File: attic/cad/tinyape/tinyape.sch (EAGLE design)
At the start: 23 parts

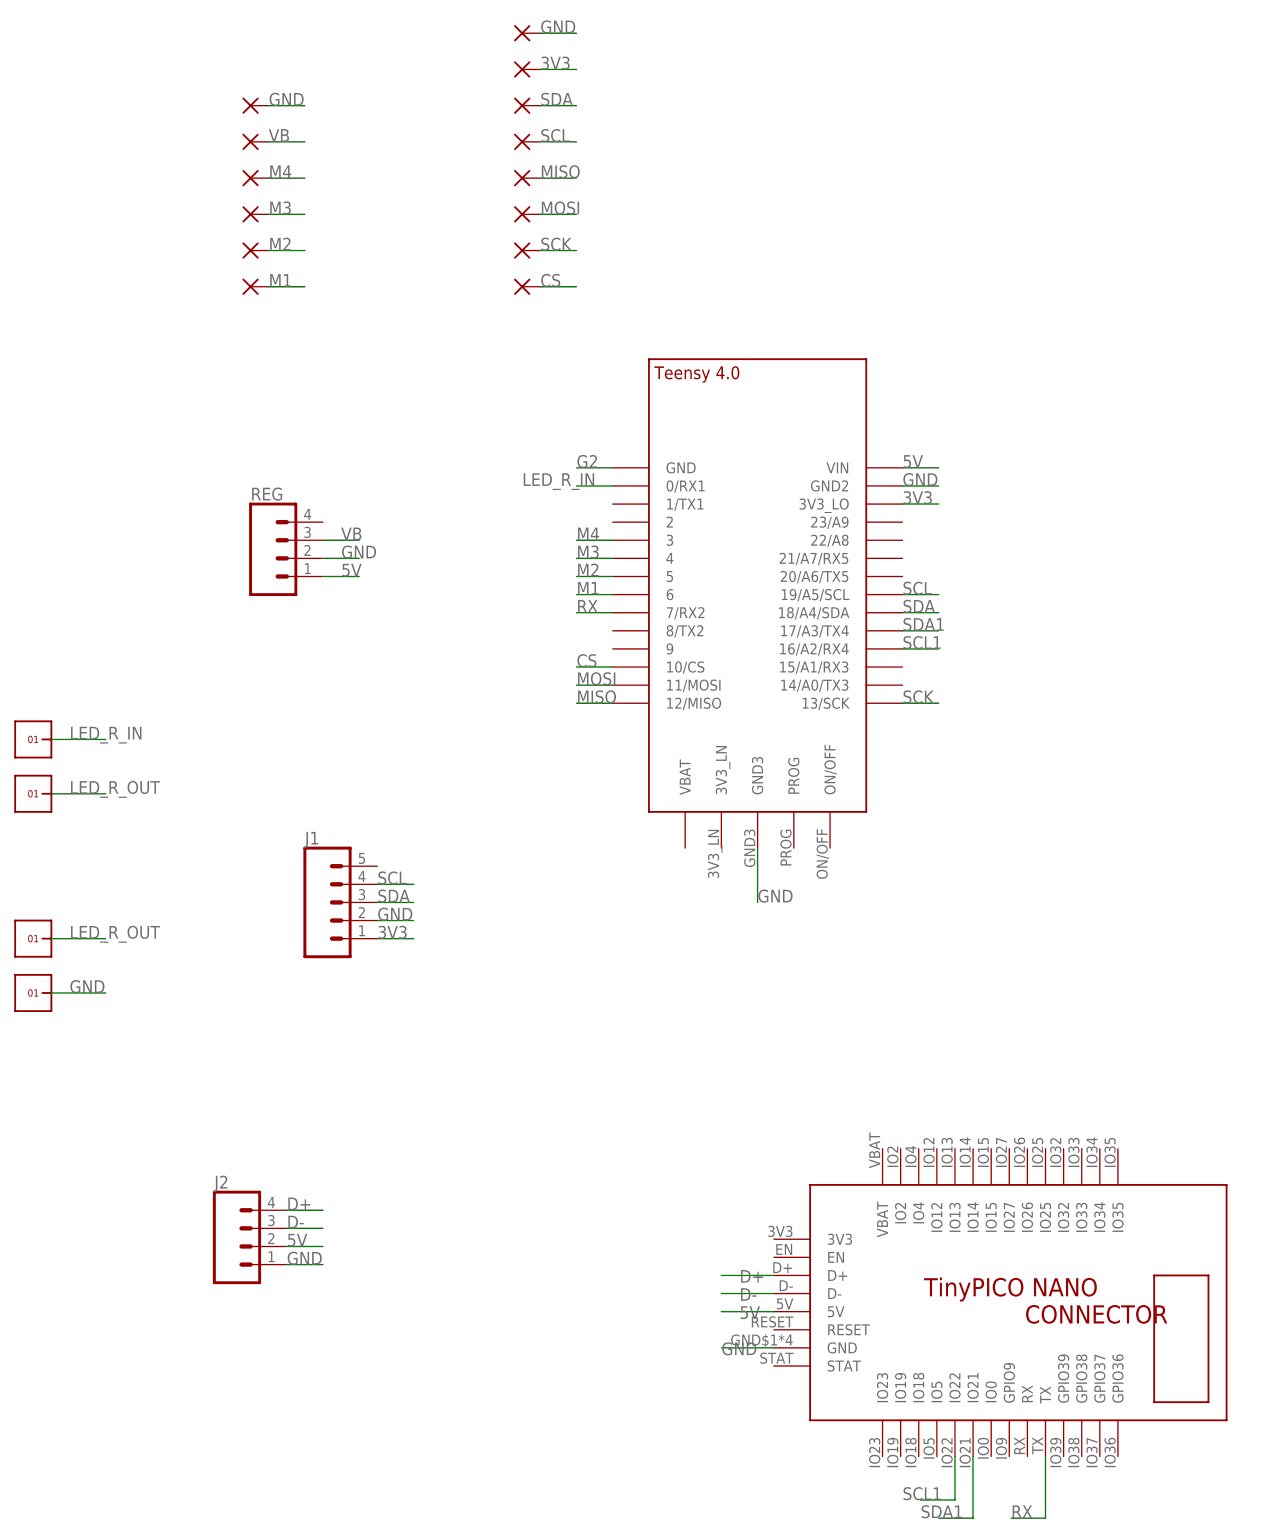
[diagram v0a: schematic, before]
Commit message: new file:   cad/fc.brd
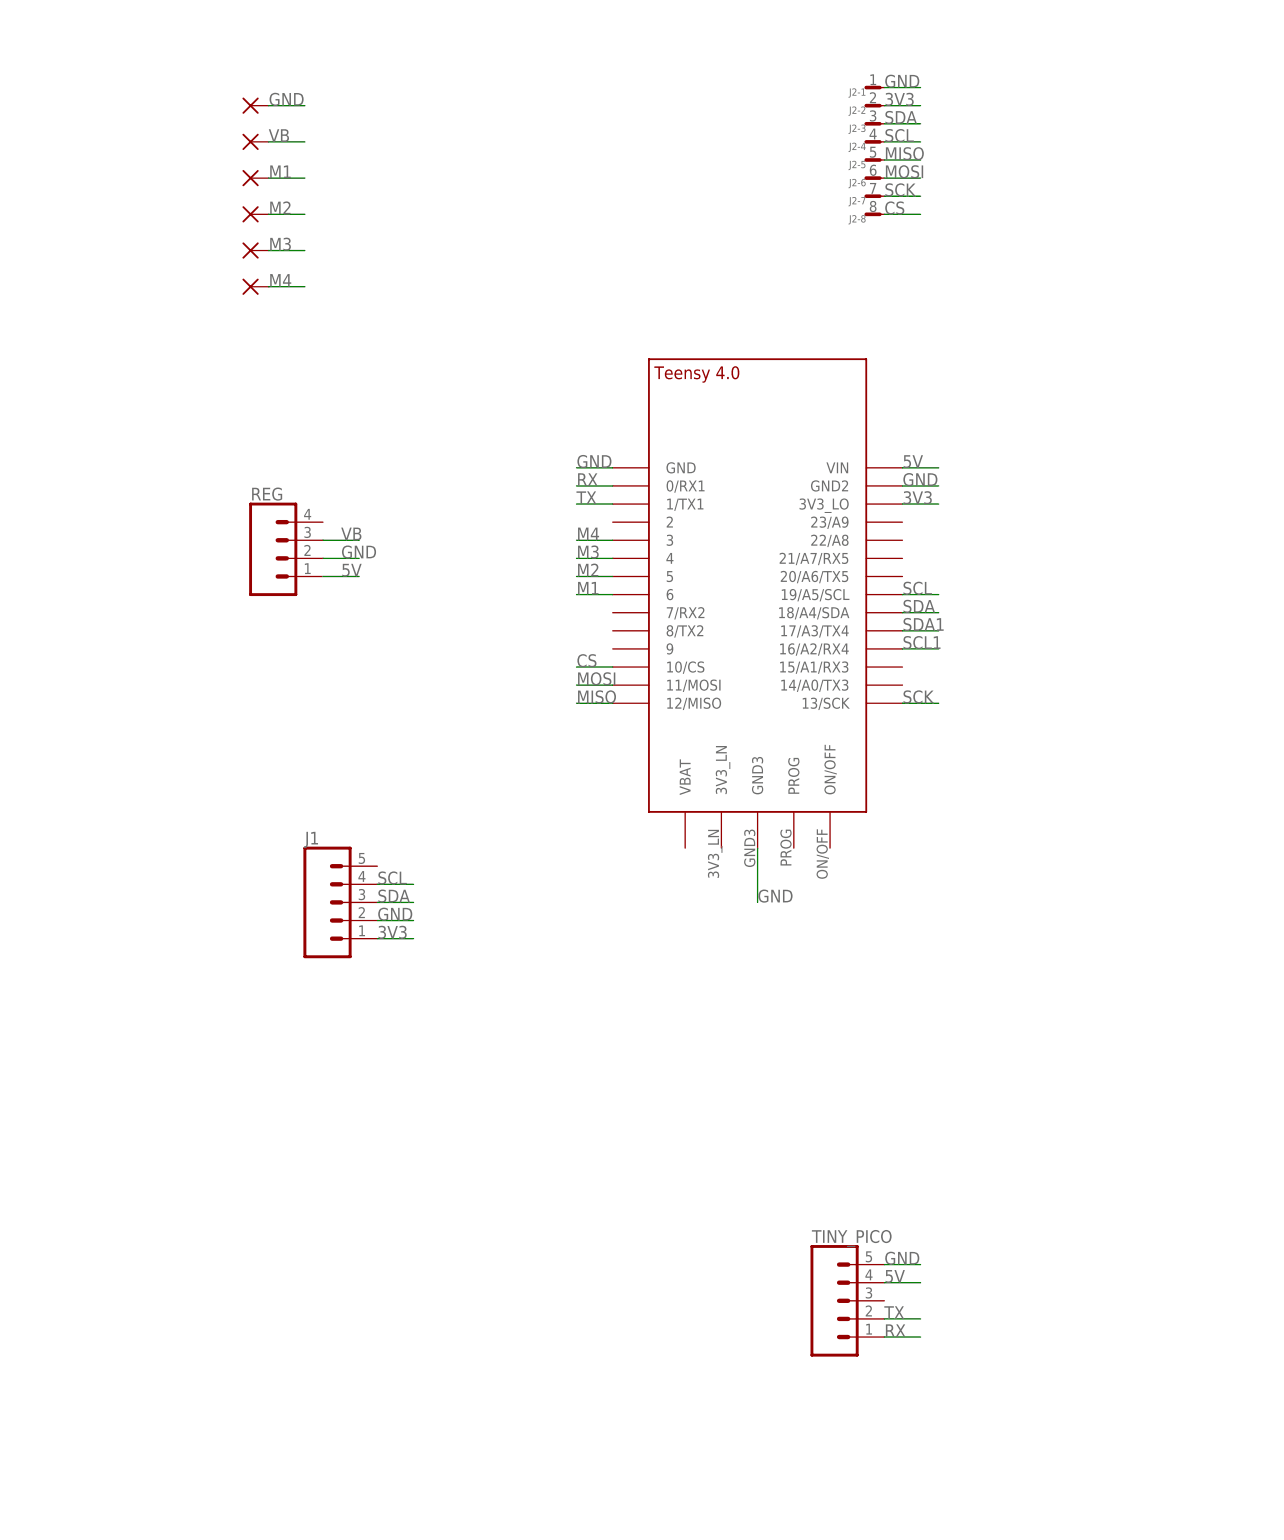
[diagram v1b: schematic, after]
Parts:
- removed 3V2, 3V3, CS, GD1, GD2, RX1, RX2, SCK: (no value), wirepad:SMD2
- removed U$2: TINYPICO-NANO-CONNECTOR, TinyPICO_NANO_Eagle:TINYPICO-NANO-CONNECTOR
- removed U$3, U$4, U$6, U$7: 1X1, headers(2mm):1X1
- added TINY_PICO: (no value), SparkFun-Connectors:CONN_05NO_SILK
- J2: value (none) -> JST-SH-8_RA; device SparkFun-Connectors:CONN_041X04_NO_SILK -> con-JST-SH:JST-SH-8_RA
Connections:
- removed net D+: J2.4, U$2.D+
- removed net D-: J2.3, U$2.D-
- removed net G2: U$1.GND
- removed net LED_R_IN: U$1.0/RX1, U$3.1
- removed net LED_R_OUT: U$4.1, U$6.1
- new net TX: TINY_PICO.2, U$1.1/TX1
- net 3V3: now also J2-2.P; no longer 3V2.P
- net 5V: now also TINY_PICO.4; no longer J2.2, U$2.5V
- net CS: now also J2-8.P; no longer CS.P
- net GND: now also J2-1.P, TINY_PICO.5, U$1.GND; no longer GD1.P, J2.1, U$2.GND, U$7.1
- net M1: now also M4.P; no longer M1.P
- net M2: now also M3.P; no longer M2.P
- net M3: now also M2.P; no longer M3.P
- net M4: now also M1.P; no longer M4.P
- net MISO: now also J2-5.P; no longer 3V3.P
- net MOSI: now also J2-6.P; no longer RX2.P
- net RX: now also TINY_PICO.1, U$1.0/RX1; no longer U$1.7/RX2, U$2.TX
- net SCK: now also J2-7.P; no longer SCK.P
- net SCL: now also J2-4.P; no longer GD2.P
- net SCL1: no longer U$2.IO22
- net SDA: now also J2-3.P; no longer RX1.P
- net SDA1: no longer U$2.IO21
